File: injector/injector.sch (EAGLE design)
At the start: 3 parts, among them J1 POWER_JACKPTH

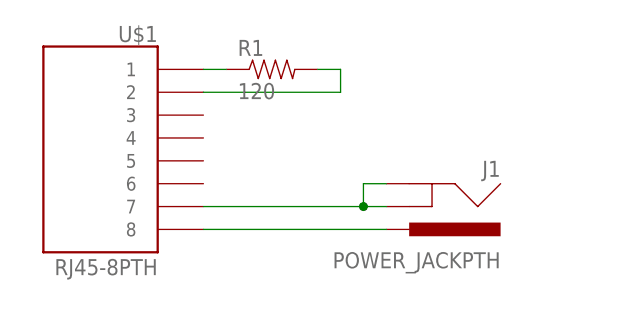
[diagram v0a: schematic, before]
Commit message: Modify injector for split termination
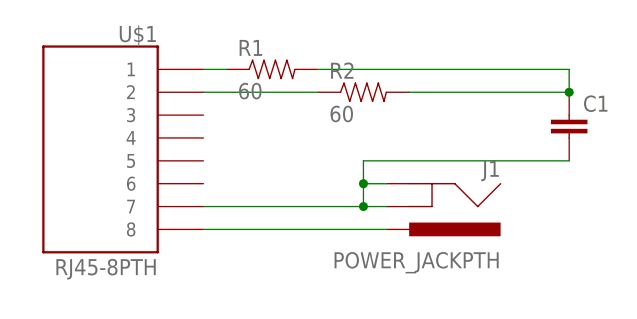
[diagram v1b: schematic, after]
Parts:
- added C1: (no value), SparkFun-Capacitors:CAP0603-CAP
- added R2: 60, SparkFun-Passives:RESISTOR0603-RES
- R1: value 120 -> 60
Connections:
- new net N$5: C1.1, R1.2, R2.2
- net N$2: now also R2.1; no longer R1.2
- net N$4: now also C1.2
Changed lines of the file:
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@@
 <parts>
 <part name="U$1" library="SparkFun-Connectors" deviceset="RJ45-8" device="PTH"/>
-<part name="R1" library="SparkFun-Passives" deviceset="RESISTOR" device="0603-RES" value="120"/>
+<part name="R1" library="SparkFun-Passives" deviceset="RESISTOR" device="0603-RES" value="60"/>
 <part name="J1" library="SparkFun-Connectors" deviceset="POWER_JACK" device="PTH"/>
+<part name="R2" library="SparkFun-Passives" deviceset="RESISTOR" device="0603-RES" value="60"/>
+<part name="C1" library="SparkFun-Capacitors" deviceset="CAP" device="0603-CAP"/>
 </parts>
 <sheets>
@@
 <instance part="R1" gate="G$1" x="33.02" y="50.8"/>
 <instance part="J1" gate="G$1" x="48.26" y="40.64" rot="R180"/>
+<instance part="R2" gate="G$1" x="43.18" y="48.26"/>
+<instance part="C1" gate="G$1" x="66.04" y="43.18"/>
 </instances>
 <busses>
 </busses>
 <nets>
-<net name="N$1" class="0">
-<segment>
-<pinref part="U$1" gate="G$1" pin="1"/>
-<pinref part="R1" gate="G$1" pin="1"/>
-<wire x1="25.4" y1="50.8" x2="27.94" y2="50.8" width="0.1524" layer="91"/>
-</segment>
-</net>
-<net name="N$2" class="0">
-<segment>
-<pinref part="R1" gate="G$1" pin="2"/>
-<wire x1="38.1" y1="50.8" x2="40.64" y2="50.8" width="0.1524" layer="91"/>
-<wire x1="40.64" y1="50.8" x2="40.64" y2="48.26" width="0.1524" layer="91"/>
-<pinref part="U$1" gate="G$1" pin="2"/>
-<wire x1="40.64" y1="48.26" x2="25.4" y2="48.26" width="0.1524" layer="91"/>
-</segment>
-</net>
 <net name="N$3" class="0">
 <segment>
@@
 <wire x1="43.18" y1="38.1" x2="43.18" y2="35.56" width="0.1524" layer="91"/>
 <junction x="43.18" y="35.56"/>
+<pinref part="C1" gate="G$1" pin="2"/>
+<wire x1="66.04" y1="40.64" x2="43.18" y2="40.64" width="0.1524" layer="91"/>
+<wire x1="43.18" y1="40.64" x2="43.18" y2="38.1" width="0.1524" layer="91"/>
+<junction x="43.18" y="38.1"/>
 </segment>
 </net>
+<net name="N$1" class="0">
+<segment>
+<pinref part="U$1" gate="G$1" pin="1"/>
+<pinref part="R1" gate="G$1" pin="1"/>
+<wire x1="25.4" y1="50.8" x2="27.94" y2="50.8" width="0.1524" layer="91"/>
+</segment>
+</net>
+<net name="N$2" class="0">
+<segment>
+<pinref part="U$1" gate="G$1" pin="2"/>
+<pinref part="R2" gate="G$1" pin="1"/>
+<wire x1="25.4" y1="48.26" x2="38.1" y2="48.26" width="0.1524" layer="91"/>
+</segment>
+</net>
+<net name="N$5" class="0">
+<segment>
+<pinref part="R2" gate="G$1" pin="2"/>
+<pinref part="C1" gate="G$1" pin="1"/>
+<wire x1="48.26" y1="48.26" x2="66.04" y2="48.26" width="0.1524" layer="91"/>
+<pinref part="R1" gate="G$1" pin="2"/>
+<wire x1="38.1" y1="50.8" x2="66.04" y2="50.8" width="0.1524" layer="91"/>
+<wire x1="66.04" y1="50.8" x2="66.04" y2="48.26" width="0.1524" layer="91"/>
+<junction x="66.04" y="48.26"/>
+</segment>
+</net>

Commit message: Minor changes to shield, rpi board, and cape
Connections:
- net N$3: now also U$1.4, U$1.5; no longer U$1.8
- net N$4: now also U$1.8
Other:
- moved on the sheet: J1
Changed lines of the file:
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@@
 <instance part="U$1" gate="G$1" x="12.7" y="40.64" rot="MR0"/>
 <instance part="R1" gate="G$1" x="33.02" y="50.8"/>
-<instance part="J1" gate="G$1" x="48.26" y="40.64" rot="R180"/>
+<instance part="J1" gate="G$1" x="48.26" y="38.1" rot="R180"/>
 <instance part="R2" gate="G$1" x="43.18" y="48.26"/>
 <instance part="C1" gate="G$1" x="66.04" y="43.18"/>
@@
 </busses>
 <nets>
-<net name="N$3" class="0">
-<segment>
-<pinref part="U$1" gate="G$1" pin="8"/>
-<pinref part="J1" gate="G$1" pin="PWR"/>
-<wire x1="25.4" y1="33.02" x2="45.72" y2="33.02" width="0.1524" layer="91"/>
-</segment>
-</net>
 <net name="N$4" class="0">
 <segment>
-<pinref part="J1" gate="G$1" pin="GNDBREAK"/>
-<pinref part="U$1" gate="G$1" pin="7"/>
-<wire x1="45.72" y1="35.56" x2="43.18" y2="35.56" width="0.1524" layer="91"/>
-<pinref part="J1" gate="G$1" pin="GND"/>
-<wire x1="43.18" y1="35.56" x2="25.4" y2="35.56" width="0.1524" layer="91"/>
-<wire x1="45.72" y1="38.1" x2="43.18" y2="38.1" width="0.1524" layer="91"/>
-<wire x1="43.18" y1="38.1" x2="43.18" y2="35.56" width="0.1524" layer="91"/>
-<junction x="43.18" y="35.56"/>
 <pinref part="C1" gate="G$1" pin="2"/>
 <wire x1="66.04" y1="40.64" x2="43.18" y2="40.64" width="0.1524" layer="91"/>
-<wire x1="43.18" y1="40.64" x2="43.18" y2="38.1" width="0.1524" layer="91"/>
-<junction x="43.18" y="38.1"/>
+<wire x1="43.18" y1="40.64" x2="43.18" y2="35.56" width="0.1524" layer="91"/>
+<pinref part="U$1" gate="G$1" pin="8"/>
+<wire x1="43.18" y1="35.56" x2="43.18" y2="33.02" width="0.1524" layer="91"/>
+<wire x1="43.18" y1="33.02" x2="25.4" y2="33.02" width="0.1524" layer="91"/>
+<pinref part="U$1" gate="G$1" pin="7"/>
+<wire x1="25.4" y1="35.56" x2="43.18" y2="35.56" width="0.1524" layer="91"/>
+<junction x="43.18" y="35.56"/>
+<pinref part="J1" gate="G$1" pin="GND"/>
+<wire x1="45.72" y1="35.56" x2="43.18" y2="35.56" width="0.1524" layer="91"/>
+<pinref part="J1" gate="G$1" pin="GNDBREAK"/>
+<wire x1="45.72" y1="33.02" x2="43.18" y2="33.02" width="0.1524" layer="91"/>
+<junction x="43.18" y="33.02"/>
 </segment>
 </net>
@@
 </segment>
 </net>
+<net name="N$3" class="0">
+<segment>
+<pinref part="J1" gate="G$1" pin="PWR"/>
+<wire x1="45.72" y1="30.48" x2="27.94" y2="30.48" width="0.1524" layer="91"/>
+<wire x1="27.94" y1="30.48" x2="27.94" y2="40.64" width="0.1524" layer="91"/>
+<pinref part="U$1" gate="G$1" pin="5"/>
+<wire x1="27.94" y1="40.64" x2="25.4" y2="40.64" width="0.1524" layer="91"/>
+<pinref part="U$1" gate="G$1" pin="4"/>
+<wire x1="25.4" y1="43.18" x2="27.94" y2="43.18" width="0.1524" layer="91"/>
+<wire x1="27.94" y1="43.18" x2="27.94" y2="40.64" width="0.1524" layer="91"/>
+<junction x="27.94" y="40.64"/>
+</segment>
+</net>
